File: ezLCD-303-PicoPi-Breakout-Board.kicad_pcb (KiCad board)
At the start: 2 copper layers, 71.1 x 50.8 mm, 20 parts, among them J1 ELP-000097, J2 ELP-000029, J3 ELP-000063, J4 ELP-000094, J5 ELP-000094, J6 ELP-000098, J7 ELP-000098, U1 ELP-000052

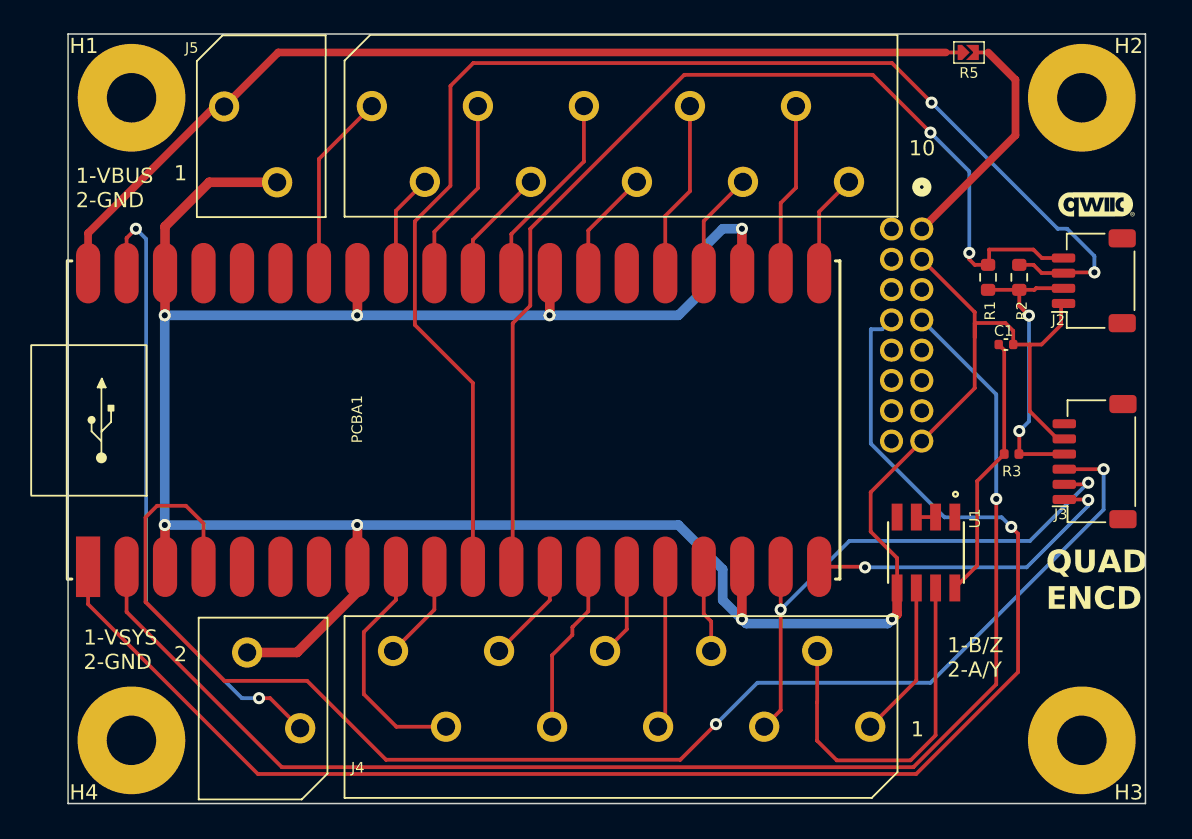
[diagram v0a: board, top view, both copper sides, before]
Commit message: Fixed errors on the schematic found after fabrication of the X1 PCB's.
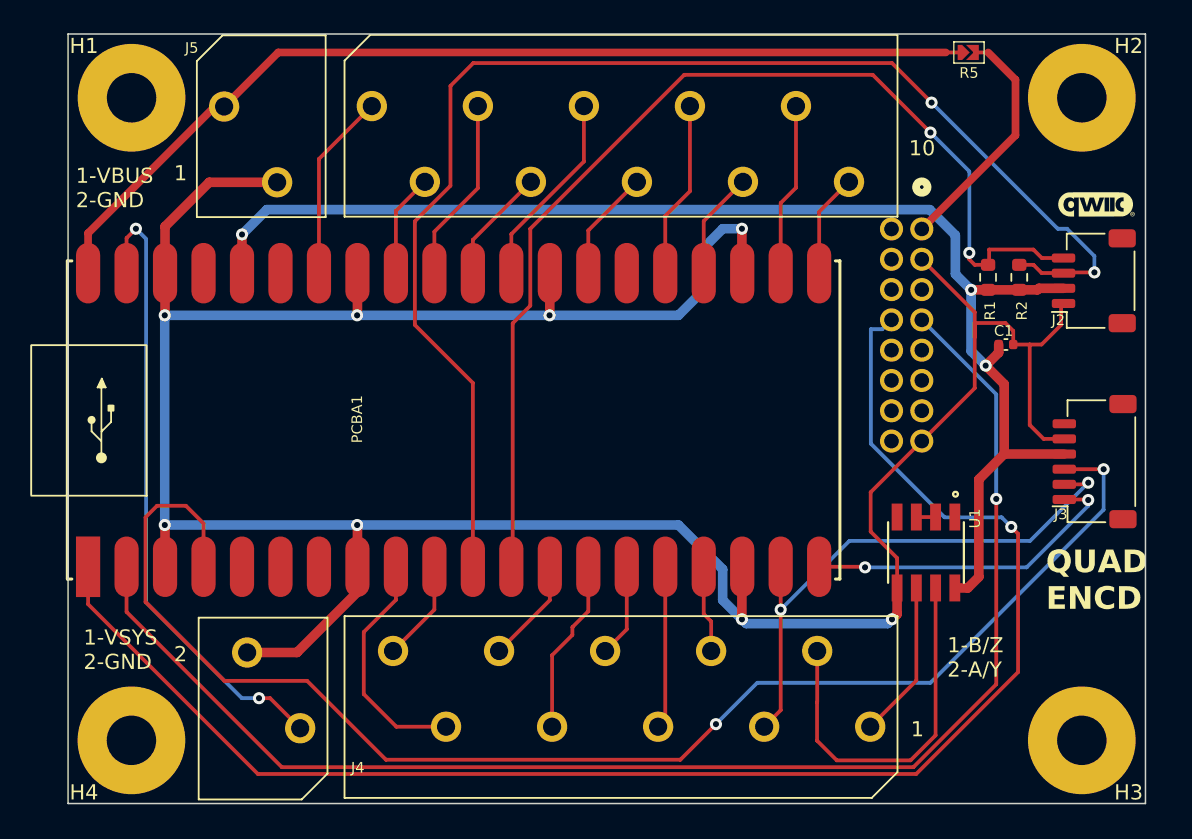
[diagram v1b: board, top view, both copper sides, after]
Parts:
- removed R3: ELP-000014, 1_EarthLCD:R_0402_1005Metric
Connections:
- C1 pad 1: Net-(U1-Vcc) -> +3.3V
- J4 pad 1: VSYS -> +3.3V
- PCBA1 pad 36: unconnected-(PCBA1-3V3(OUT)-Pad36) -> +3.3V
- U1 pad 8: Net-(U1-Vcc) -> +3.3V
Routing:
- net +3.3V: track 19.4 -> 89.4 mm, vias 2 -> 3
- net Net-(U1-Vcc): track 17.6 -> 0.00 mm
- net GND: track 198.7 -> 199.2 mm
